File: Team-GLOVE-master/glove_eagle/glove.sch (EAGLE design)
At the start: 51 parts, among them J1 MICRO_USB_B_JST_MC5BR3-M404-4S, U1 BNO055, U3 NRF51822QF, U4 MCP73831, X3 ABS05-32.768KHZ-9-T

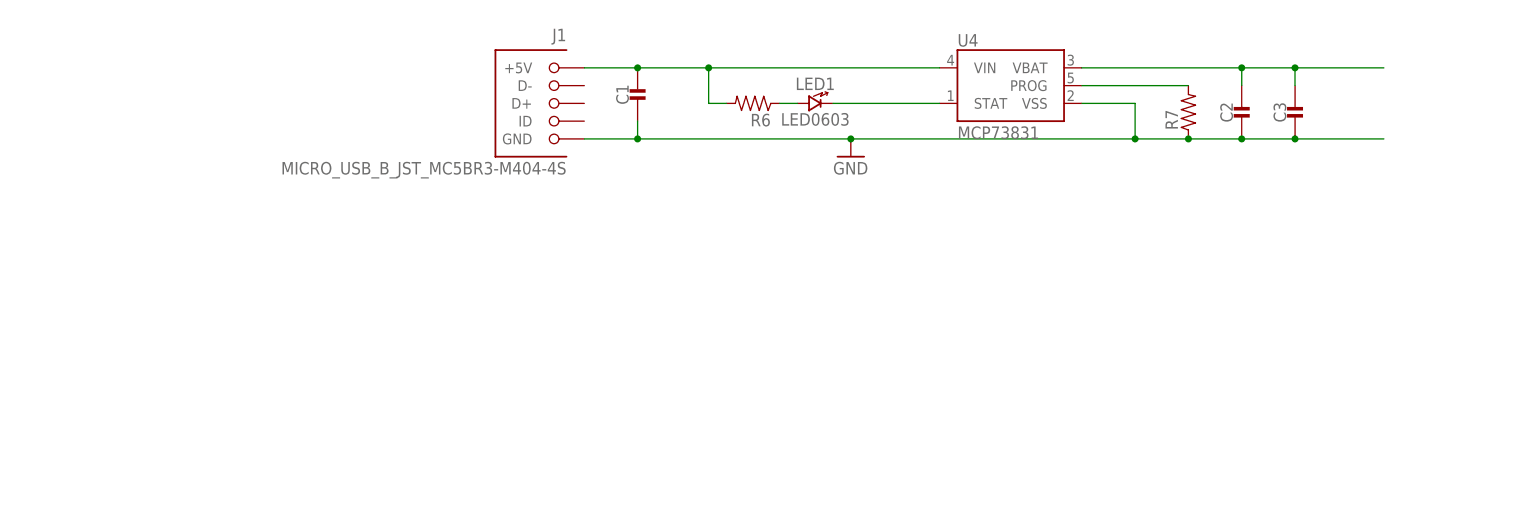
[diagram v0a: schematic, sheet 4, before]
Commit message: Finished routing nearly completed board
Still lots of modifications to make, but it's a start.
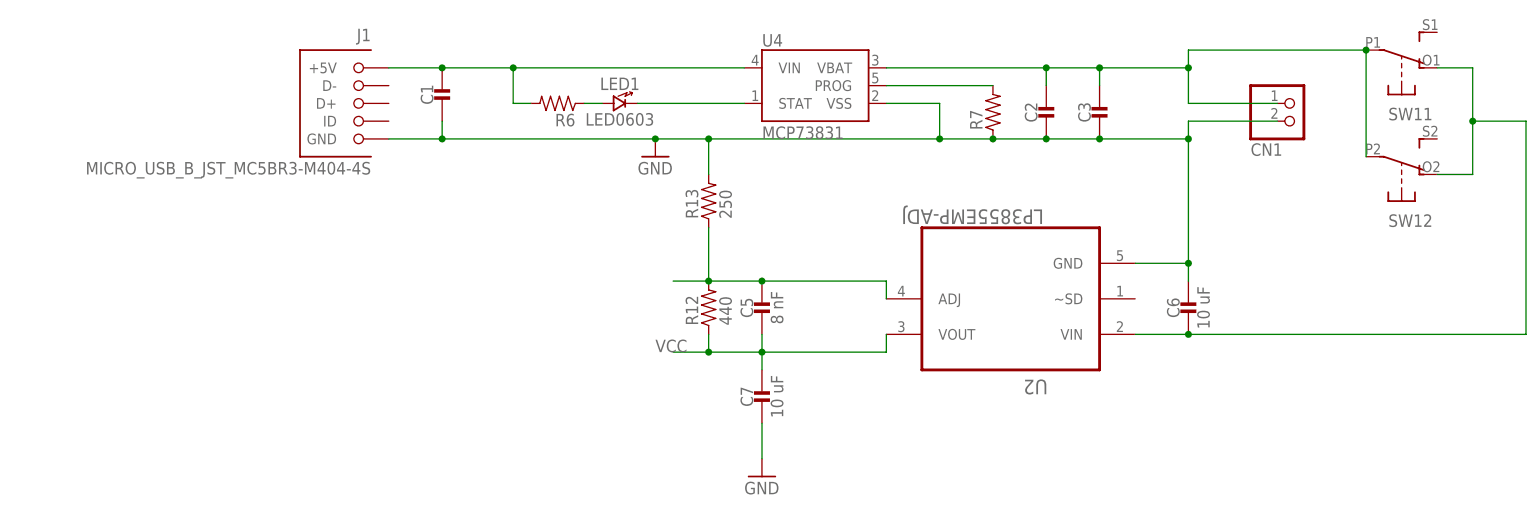
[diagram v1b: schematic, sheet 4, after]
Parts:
- removed R14: (no value), passives:RESISTOR0603_RES
- added C5: 8 nF, passives:CAPACITOR0603_CAP
- added C6, C7: 10 uF, passives:CAPACITOR0603_CAP
- added CN1: (no value), adafruit:JST_2PIN-SMT-RA
- added SW1: (no value), adafruit:DPDT-EG1390
- added U2: LP3855EMP-ADJ, LP3855EMP-ADJ:LP3855EMP-ADJ
- R12: value (none) -> 440
- R13: value (none) -> 250
- R15, R16, R17, R18: value (none) -> 10 k
- R9: value (none) -> 47 k
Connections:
- removed net N$10: R13.1
- removed net N$11: R14.2, U$1.KEY4
- removed net N$13: R14.1
- removed net N$6: R12.2, U$1.KEY6
- removed net N$8: R13.2, U$1.KEY5
- new net N$5: C6.2, SW11.O, SW12.O, U2.VIN
- net GND: now also C6.1, C7.2, CN1.1, R13.2, U2.GND
- net N$1: now also CN1.2, SW11.P, SW12.P
- net N$7: now also C5.1, R12.2, R13.1, U2.ADJ; no longer R12.1
- net VCC: now also C5.2, C7.1, R12.1, U2.VOUT
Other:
- moved on the sheet: C1, C2, C3, J1, LED1, R10, R6, R7, U4
